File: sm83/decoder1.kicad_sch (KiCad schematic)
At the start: 213 parts

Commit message: SM83: Add schematic of decoder2
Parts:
- removed U?: NOT_OD, symbol SM83_Decoders:NOT_OD
- added U?: NOT_OD, symbol SM83_Decoders:NOT_OD
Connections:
- net at U?.1, U?.5: now also U?.1
- new net: DEC1_NOT8. (B_Y), U?.2
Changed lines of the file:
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@@
 	)
 	(symbol
-		(lib_id "SM83_Decoders:NOT_OD")
-		(at 96.52 373.38 0)
-		(unit 1)
-		(exclude_from_sim no)
-		(in_bom yes)
-		(on_board yes)
-		(dnp no)
-		(property "Reference" "U?"
-			(at 96.52 368.3 0)
-			(effects
-				(font
-					(size 1.27 1.27)
-				)
-				(hide yes)
-			)
-		)
-		(property "Value" "NOT_OD"
-			(at 96.52 378.46 0)
-			(effects
-				(font
-					(size 1.27 1.27)
-				)
-				(hide yes)
-			)
-		)
-		(property "Footprint" ""
-			(at 93.98 373.38 0)
-			(effects
-				(font
-					(size 1.27 1.27)
-				)
-				(hide yes)
-			)
-		)
-		(property "Datasheet" ""
-			(at 96.52 381 0)
-			(effects
-				(font
-					(size 1.27 1.27)
-				)
-				(hide yes)
-			)
-		)
-		(property "Description" "Open-drain inverter."
-			(at 96.52 383.54 0)
-			(effects
-				(font
-					(size 1.27 1.27)
-				)
-				(hide yes)
-			)
-		)
-		(pin "1"
-		)
-		(pin "2"
-		)
-		(instances
-			(project ""
-				(path "/8717d046-1dfd-46fe-a5f7-4e4d2f07de68/88dfb20a-107a-45c1-8e80-cb3f4ae5577b"
-					(reference "U?")
-					(unit 1)
-				)
-			)
-		)
-	)
-	(symbol
 		(lib_id "SM83_Decoders:AND4")
 		(at 213.36 234.95 0)
@@
 				(path "/8717d046-1dfd-46fe-a5f7-4e4d2f07de68/88dfb20a-107a-45c1-8e80-cb3f4ae5577b"
 					(reference "U?")
+					(unit 1)
+				)
+			)
+		)
+	)
+	(symbol
+		(lib_id "SM83_Decoders:NOT_OD")
+		(at 96.52 373.38 0)
+		(unit 1)
+		(exclude_from_sim no)
+		(in_bom yes)
+		(on_board yes)
+		(dnp no)
+		(property "Reference" "U?"
+			(at 96.52 368.3 0)
+			(effects
+				(font
+					(size 1.27 1.27)
+				)
+				(hide yes)
+			)
+		)
+		(property "Value" "NOT_OD"
+			(at 96.52 378.46 0)
+			(effects
+				(font
+					(size 1.27 1.27)
+				)
+				(hide yes)
+			)
+		)
+		(property "Footprint" ""
+			(at 93.98 373.38 0)
+			(effects
+				(font
+					(size 1.27 1.27)
+				)
+				(hide yes)
+			)
+		)
+		(property "Datasheet" ""
+			(at 96.52 381 0)
+			(effects
+				(font
+					(size 1.27 1.27)
+				)
+				(hide yes)
+			)
+		)
+		(property "Description" "Open-drain inverter."
+			(at 96.52 383.54 0)
+			(effects
+				(font
+					(size 1.27 1.27)
+				)
+				(hide yes)
+			)
+		)
+		(pin "2"
+		)
+		(pin "1"
+		)
+		(instances
+			(project ""
+				(path "/8717d046-1dfd-46fe-a5f7-4e4d2f07de68/88dfb20a-107a-45c1-8e80-cb3f4ae5577b"
+					(reference "U?")

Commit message: SM83: Add schematic for decoder3
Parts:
- added DEC1_NOT57, DEC1_NOT58, DEC1_NOT59, DEC1_NOT60, DEC1_NOT61, DEC1_NOT62, DEC1_NOT63, DEC1_NOT64: NOT_DEC1, symbol SM83_Cells:NOT_DEC1
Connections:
- net OPCODE0: now also DEC1_NOT64.1
- net OPCODE1: now also DEC1_NOT63.1
- net OPCODE2: now also DEC1_NOT62.1
- net OPCODE3: now also DEC1_NOT61.1
- net OPCODE4: now also DEC1_NOT60.1
- net OPCODE5: now also DEC1_NOT59.1
- net OPCODE6: now also DEC1_NOT58.1
- net OPCODE7: now also DEC1_NOT57.1
- net ~{OPCODE0}: now also DEC1_NOT64.2
- net ~{OPCODE1}: now also DEC1_NOT63.2
- net ~{OPCODE2}: now also DEC1_NOT62.2
- net ~{OPCODE3}: now also DEC1_NOT61.2
- net ~{OPCODE4}: now also DEC1_NOT60.2
- net ~{OPCODE5}: now also DEC1_NOT59.2
- net ~{OPCODE6}: now also DEC1_NOT58.2
- net ~{OPCODE7}: now also DEC1_NOT57.2

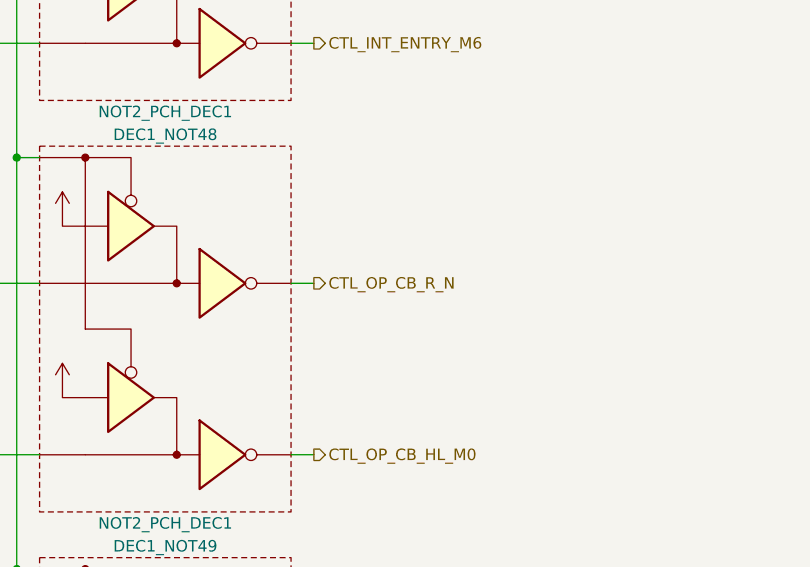
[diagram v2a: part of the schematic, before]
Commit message: Finish SM83 CPU schematic
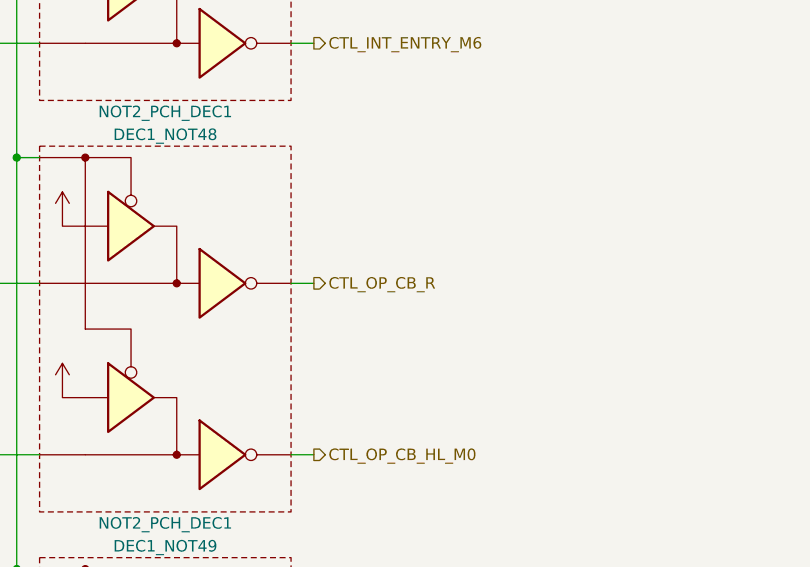
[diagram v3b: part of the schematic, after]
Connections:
- net CTL_OP_CB_R_N is gone; now on net EXEC_PHASE: DEC1_NOT48. (B_Y)
- new net CTL_OP_CB_R: DEC1_NOT48. (B_Y)
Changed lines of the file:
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@@
 	(title_block
 		(title "SM83 CPU")
-		(date "2025-12-08")
+		(date "2025-12-24")
 		(rev "0")
 		(company "CC-BY-SA-4.0 Michael Singer")
@@
 		)
 	)
-	(hierarchical_label "CTL_OP_CB_R_N"
+	(hierarchical_label "CTL_OP_CB_R"
 		(shape output)
 		(at 444.5 591.82 0)
